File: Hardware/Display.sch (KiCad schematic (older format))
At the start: 10 parts

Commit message: [Hardware] Added buttons.
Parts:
- removed Q?: BD135, Package_TO_SOT_THT:TO-126-3_Vertical, symbol Transistor_BJT:BD135
- added Q1: DMG3414U, Package_TO_SOT_SMD:SOT-23, symbol Transistor_FET:DMG3414U
- R8: renamed from R?; value 1K -> 10K
- gave numbers to parts that had none: 7
- renumbered 10K to 10K1
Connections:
- wire segments 49 -> 53
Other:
- moved on the sheet: R8
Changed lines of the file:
@@
 $EndDescr
 $Comp
-L Transistor_BJT:BD135 Q?
-U 1 1 5E7D0088
-P 5750 5350
-F 0 "Q?" H 5941 5396 50  0000 L CNN
-F 1 "BD135" H 5941 5305 50  0000 L CNN
-F 2 "Package_TO_SOT_THT:TO-126-3_Vertical" H 5950 5275 50  0001 L CIN
-F 3 "http://www.st.com/internet/com/TECHNICAL_RESOURCES/TECHNICAL_LITERATURE/DATASHEET/CD00001225.pdf" H 5750 5350 50  0001 L CNN
-	1    5750 5350
-	-1   0    0    -1
-$EndComp
-$Comp
-L Connector:Conn_01x06_Male J?
+L Connector:Conn_01x06_Male J3
 U 1 1 5E7D0A45
 P 4500 2950
-F 0 "J?" H 4608 3331 50  0000 C CNN
+F 0 "J3" H 4608 3331 50  0000 C CNN
 F 1 "Conn_01x06_Male" H 4608 3240 50  0000 C CNN
 F 2 "" H 4500 2950 50  0001 C CNN
@@
 VDD
 $Comp
-L Connector:Conn_01x10_Male J?
+L Connector:Conn_01x10_Male J4
 U 1 1 5E7D7996
 P 4500 4050
-F 0 "J?" H 4608 4631 50  0000 C CNN
+F 0 "J4" H 4608 4631 50  0000 C CNN
 F 1 "Conn_01x10_Male" H 4608 4540 50  0000 C CNN
 F 2 "" H 4500 4050 50  0001 C CNN
@@
 LED+
 $Comp
-L power:GND #PWR?
+L power:GND #PWR0119
 U 1 1 5E7DC996
 P 5800 2400
-F 0 "#PWR?" H 5800 2150 50  0001 C CNN
+F 0 "#PWR0119" H 5800 2150 50  0001 C CNN
 F 1 "GND" H 5805 2227 50  0000 C CNN
 F 2 "" H 5800 2400 50  0001 C CNN
@@
 P 5300 2650
 AR Path="/5E7E4239" Ref="C?"  Part="1"
-AR Path="/5E7CFAFC/5E7E4239" Ref="C?"  Part="1"
-F 0 "C?" H 5415 2787 50  0000 L CNN
+AR Path="/5E7CFAFC/5E7E4239" Ref="C7"  Part="1"
+F 0 "C7" H 5415 2787 50  0000 L CNN
 F 1 "100n" H 5415 2696 50  0000 L CNN
 F 2 "Capacitor_SMD:C_1206_3216Metric_Pad1.42x1.75mm_HandSolder" H 5338 2500 50  0001 C CNN
@@
 $EndComp
 $Comp
-L Device:R_POT_TRIM 10K
+L Device:R_POT_TRIM 10K1
 U 1 1 5E7DEAB7
 P 6950 2650
-F 0 "10K" H 6880 2696 50  0000 R CNN
+F 0 "10K1" H 6880 2696 50  0000 R CNN
 F 1 "R_POT_TRIM" H 7450 2850 50  0000 R CNN
 F 2 "" H 6950 2650 50  0001 C CNN
@@
 P 5800 2650
 AR Path="/5E7EC9B4" Ref="C?"  Part="1"
-AR Path="/5E7CFAFC/5E7EC9B4" Ref="C?"  Part="1"
-F 0 "C?" H 5915 2787 50  0000 L CNN
+AR Path="/5E7CFAFC/5E7EC9B4" Ref="C8"  Part="1"
+F 0 "C8" H 5915 2787 50  0000 L CNN
 F 1 "470n" H 5915 2696 50  0000 L CNN
 F 2 "Capacitor_SMD:C_1206_3216Metric_Pad1.42x1.75mm_HandSolder" H 5838 2500 50  0001 C CNN
@@
 $EndComp
 $Comp
-L Device:CP C?
+L Device:CP C9
 U 1 1 5E7EE2A7
 P 6300 2650
-F 0 "C?" H 6182 2559 50  0000 R CNN
+F 0 "C9" H 6182 2559 50  0000 R CNN
 F 1 "220u" H 6182 2650 50  0000 R CNN
 F 2 "" H 6338 2500 50  0001 C CNN
@@
 	7100 2850 6950 2850
 $Comp
-L power:+5V #PWR?
+L power:+5V #PWR0120
 U 1 1 5E7DD692
 P 7100 2850
-F 0 "#PWR?" H 7100 2700 50  0001 C CNN
+F 0 "#PWR0120" H 7100 2700 50  0001 C CNN
 F 1 "+5V" V 7115 2978 50  0000 L CNN
 F 2 "" H 7100 2850 50  0001 C CNN
@@
 DISPLAY_DB7
 $Comp
-L power:+5V #PWR?
+L power:+5V #PWR0121
 U 1 1 5E821DC4
 P 4850 4550
-F 0 "#PWR?" H 4850 4400 50  0001 C CNN
+F 0 "#PWR0121" H 4850 4400 50  0001 C CNN
 F 1 "+5V" V 4865 4678 50  0000 L CNN
 F 2 "" H 4850 4550 50  0001 C CNN
@@
 AR Path="/5E7ACE5B/5E82967A" Ref="R?"  Part="1"
 AR Path="/5E82967A" Ref="R?"  Part="1"
-AR Path="/5E7CFAFC/5E82967A" Ref="R?"  Part="1"
-F 0 "R?" H 5430 4804 50  0000 R CNN
+AR Path="/5E7CFAFC/5E82967A" Ref="R6"  Part="1"
+F 0 "R6" H 5430 4804 50  0000 R CNN
 F 1 "12" H 5430 4895 50  0000 R CNN
 F 2 "Resistor_SMD:R_1206_3216Metric_Pad1.42x1.75mm_HandSolder" V 5430 4850 50  0001 C CNN
@@
 	-1   0    0    1
 $EndComp
-Wire Wire Line
-	5650 5050 5650 5150
-$Comp
-L power:GND #PWR?
+$Comp
+L power:GND #PWR0122
 U 1 1 5E82B8E8
-P 5650 5650
-F 0 "#PWR?" H 5650 5400 50  0001 C CNN
-F 1 "GND" H 5655 5477 50  0000 C CNN
-F 2 "" H 5650 5650 50  0001 C CNN
-F 3 "" H 5650 5650 50  0001 C CNN
-	1    5650 5650
+P 5650 5850
+F 0 "#PWR0122" H 5650 5600 50  0001 C CNN
+F 1 "GND" H 5655 5677 50  0000 C CNN
+F 2 "" H 5650 5850 50  0001 C CNN
+F 3 "" H 5650 5850 50  0001 C CNN
+	1    5650 5850
 	1    0    0    -1
 $EndComp
@@
 L Device:R R?
 U 1 1 5E82D0F5
-P 6200 5350
+P 6150 5600
 AR Path="/5E7ACE5B/5E82D0F5" Ref="R?"  Part="1"
 AR Path="/5E82D0F5" Ref="R?"  Part="1"
-AR Path="/5E7CFAFC/5E82D0F5" Ref="R?"  Part="1"
-F 0 "R?" V 6407 5350 50  0000 C CNN
-F 1 "1K" V 6316 5350 50  0000 C CNN
-F 2 "Resistor_SMD:R_1206_3216Metric_Pad1.42x1.75mm_HandSolder" V 6130 5350 50  0001 C CNN
-F 3 "~" H 6200 5350 50  0001 C CNN
-	1    6200 5350
-	0    -1   -1   0
-$EndComp
-Wire Wire Line
-	5950 5350 6050 5350
-Text HLabel 6500 5350 2    50   Input ~ 0
+AR Path="/5E7CFAFC/5E82D0F5" Ref="R8"  Part="1"
+F 0 "R8" H 6220 5646 50  0000 L CNN
+F 1 "10K" H 6220 5555 50  0000 L CNN
+F 2 "Resistor_SMD:R_1206_3216Metric_Pad1.42x1.75mm_HandSolder" V 6080 5600 50  0001 C CNN
+F 3 "~" H 6150 5600 50  0001 C CNN
+	1    6150 5600
+	1    0    0    -1
+$EndComp
+Text HLabel 6500 5400 2    50   Input ~ 0
 DISPLAY_BACKLIGHT
 Wire Wire Line
-	6350 5350 6500 5350
-Wire Wire Line
-	5650 5550 5650 5650
+	5650 5600 5650 5800
 $Comp
 L Device:R R?
@@
 AR Path="/5E7ACE5B/5E836C01" Ref="R?"  Part="1"
 AR Path="/5E836C01" Ref="R?"  Part="1"
-AR Path="/5E7CFAFC/5E836C01" Ref="R?"  Part="1"
-F 0 "R?" H 5730 4804 50  0000 R CNN
+AR Path="/5E7CFAFC/5E836C01" Ref="R7"  Part="1"
+F 0 "R7" H 5730 4804 50  0000 R CNN
 F 1 "12" H 5730 4895 50  0000 R CNN
 F 2 "Resistor_SMD:R_1206_3216Metric_Pad1.42x1.75mm_HandSolder" V 5730 4850 50  0001 C CNN
@@
 Text Notes 6400 4950 0    50   ~ 0
 Backlight leds forward voltage is about 4 to 4.5V.\nBacklight leds maximum current is 200mA.\nWith 6 ohm resistor, maximum current will be\nbetween (5-4)/6 = 166mA and (5-4.5)/6 = 83mA.\nResistors dissipated power is between\n(5-4)²/6 = 166mW and (5-4.5)²/6 = 42mW,\nso allow up to 500mW to be dissipated to be sure.
+$Comp
+L Transistor_FET:DMG3414U Q1
+U 1 1 5E7C7532
+P 5750 5400
+F 0 "Q1" H 5956 5446 50  0000 L CNN
+F 1 "DMG3414U" H 5956 5355 50  0000 L CNN
+F 2 "Package_TO_SOT_SMD:SOT-23" H 5950 5325 50  0001 L CIN
+F 3 "http://www.diodes.com/assets/Datasheets/ds31739.pdf" H 5750 5400 50  0001 L CNN
+	1    5750 5400
+	-1   0    0    -1
+$EndComp
+Wire Wire Line
+	5650 5800 6150 5800
+Wire Wire Line
+	6150 5800 6150 5750
+Connection ~ 5650 5800
+Wire Wire Line
+	5650 5800 5650 5850
+Wire Wire Line
+	5950 5400 6150 5400
+Wire Wire Line
+	6150 5400 6150 5450
+Wire Wire Line
+	6150 5400 6500 5400
+Connection ~ 6150 5400
+Wire Wire Line
+	5650 5050 5650 5200
 $EndSCHEMATC

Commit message: [Hardware] Added all schematic parts (but not all external parts, like display or female connectors).
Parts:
- C8: value 470n -> 4.7u
- C9: footprint (none) -> Capacitor_SMD:CP_Elec_8x10.5
- J3: footprint (none) -> Connector_PinHeader_2.54mm:PinHeader_1x06_P2.54mm_Vertical
- J4: footprint (none) -> Connector_PinHeader_2.54mm:PinHeader_1x10_P2.54mm_Vertical
- RV1: renamed from 10K1; value R_POT_TRIM -> 10K; footprint (none) -> Potentiometer_SMD:Potentiometer_Bourns_3314J_Vertical; Champ4 (none) -> Bourns 3314J-1-103E
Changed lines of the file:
@@
 $Descr A4 11693 8268
 encoding utf-8
-Sheet 4 3
+Sheet 3 3
 Title "4 lines x 20 characters LCD display"
 Date ""
@@
 F 0 "J3" H 4608 3331 50  0000 C CNN
 F 1 "Conn_01x06_Male" H 4608 3240 50  0000 C CNN
-F 2 "" H 4500 2950 50  0001 C CNN
+F 2 "Connector_PinHeader_2.54mm:PinHeader_1x06_P2.54mm_Vertical" H 4500 2950 50  0001 C CNN
 F 3 "~" H 4500 2950 50  0001 C CNN
 	1    4500 2950
@@
 F 0 "J4" H 4608 4631 50  0000 C CNN
 F 1 "Conn_01x10_Male" H 4608 4540 50  0000 C CNN
-F 2 "" H 4500 4050 50  0001 C CNN
+F 2 "Connector_PinHeader_2.54mm:PinHeader_1x10_P2.54mm_Vertical" H 4500 4050 50  0001 C CNN
 F 3 "~" H 4500 4050 50  0001 C CNN
 	1    4500 4050
@@
 $EndComp
 $Comp
-L Device:R_POT_TRIM 10K1
+L Device:R_POT_TRIM RV1
 U 1 1 5E7DEAB7
 P 6950 2650
-F 0 "10K1" H 6880 2696 50  0000 R CNN
-F 1 "R_POT_TRIM" H 7450 2850 50  0000 R CNN
-F 2 "" H 6950 2650 50  0001 C CNN
+F 0 "RV1" H 6881 2741 50  0000 R CNN
+F 1 "10K" H 6881 2650 50  0000 R CNN
+F 2 "Potentiometer_SMD:Potentiometer_Bourns_3314J_Vertical" H 6950 2650 50  0001 C CNN
 F 3 "~" H 6950 2650 50  0001 C CNN
+F 4 "Bourns 3314J-1-103E" H 7900 2800 50  0000 R CNN "Champ4"
 	1    6950 2650
 	1    0    0    -1
@@
 AR Path="/5E7CFAFC/5E7EC9B4" Ref="C8"  Part="1"
 F 0 "C8" H 5915 2787 50  0000 L CNN
-F 1 "470n" H 5915 2696 50  0000 L CNN
+F 1 "4.7u" H 5915 2696 50  0000 L CNN
 F 2 "Capacitor_SMD:C_1206_3216Metric_Pad1.42x1.75mm_HandSolder" H 5838 2500 50  0001 C CNN
 F 3 "~" H 5800 2650 50  0001 C CNN
@@
 F 0 "C9" H 6182 2559 50  0000 R CNN
 F 1 "220u" H 6182 2650 50  0000 R CNN
-F 2 "" H 6338 2500 50  0001 C CNN
+F 2 "Capacitor_SMD:CP_Elec_8x10.5" H 6338 2500 50  0001 C CNN
 F 3 "~" H 6300 2650 50  0001 C CNN
 F 4 "25V" H 6182 2741 50  0000 R CNN "Champ4"

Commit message: [Hardware] Started PCB routing. Components are placed, BME680 board mounting holes are in position, some nets are connected.
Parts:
- J3: value Conn_01x06_Male -> Display_1
- J4: value Conn_01x10_Male -> Display_2
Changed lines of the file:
@@
 P 4500 2950
 F 0 "J3" H 4608 3331 50  0000 C CNN
-F 1 "Conn_01x06_Male" H 4608 3240 50  0000 C CNN
+F 1 "Display_1" H 4608 3240 50  0000 C CNN
 F 2 "Connector_PinHeader_2.54mm:PinHeader_1x06_P2.54mm_Vertical" H 4500 2950 50  0001 C CNN
 F 3 "~" H 4500 2950 50  0001 C CNN
@@
 P 4500 4050
 F 0 "J4" H 4608 4631 50  0000 C CNN
-F 1 "Conn_01x10_Male" H 4608 4540 50  0000 C CNN
+F 1 "Display_2" H 4608 4540 50  0000 C CNN
 F 2 "Connector_PinHeader_2.54mm:PinHeader_1x10_P2.54mm_Vertical" H 4500 4050 50  0001 C CNN
 F 3 "~" H 4500 4050 50  0001 C CNN

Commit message: [Hardware] Moved buttons to another schematic sheet and fully routed PCB.
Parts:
- C9: Champ6 (none) -> Panasonic EEEFK1E221P
- RV1: Champ4 Bourns 3314J-1-103E -> (none); Champ6 (none) -> Bourns 3314J-1-103E
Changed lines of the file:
@@
 $Descr A4 11693 8268
 encoding utf-8
-Sheet 3 3
+Sheet 3 4
 Title "4 lines x 20 characters LCD display"
 Date ""
@@
 F 2 "Potentiometer_SMD:Potentiometer_Bourns_3314J_Vertical" H 6950 2650 50  0001 C CNN
 F 3 "~" H 6950 2650 50  0001 C CNN
-F 4 "Bourns 3314J-1-103E" H 7900 2800 50  0000 R CNN "Champ4"
+F 4 "Bourns 3314J-1-103E" H 7900 2800 50  0000 R CNN "Champ6"
 	1    6950 2650
 	1    0    0    -1
@@
 F 3 "~" H 6300 2650 50  0001 C CNN
 F 4 "25V" H 6182 2741 50  0000 R CNN "Champ4"
+F 5 "Panasonic EEEFK1E221P" H 6300 2650 50  0001 C CNN "Champ6"
 	1    6300 2650
 	-1   0    0    1

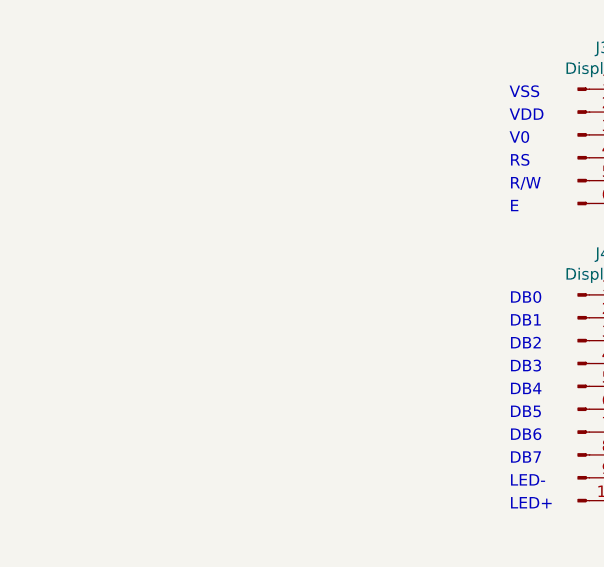
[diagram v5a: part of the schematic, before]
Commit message: [Hardware] Added display part in both schematic and PCB.
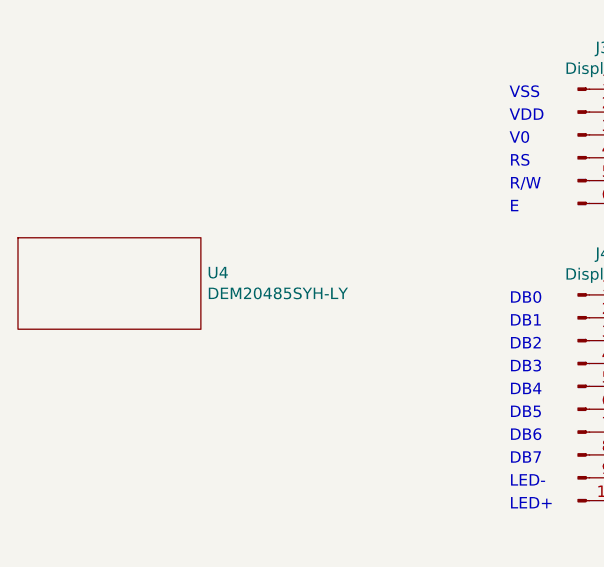
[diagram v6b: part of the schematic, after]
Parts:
- added U4: DEM20485SYH-LY, Empty_Footprint:Empty_Footprint, symbol LCD_Display:DEM20485SYH-LY
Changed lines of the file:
@@
 Wire Wire Line
 	5650 5050 5650 5200
+$Comp
+L LCD_Display:DEM20485SYH-LY U4
+U 1 1 5E7D0A49
+P 2450 3600
+F 0 "U4" H 2878 3646 50  0000 L CNN
+F 1 "DEM20485SYH-LY" H 2878 3555 50  0000 L CNN
+F 2 "Empty_Footprint:Empty_Footprint" H 2450 3600 50  0001 C CNN
+F 3 "" H 2450 3600 50  0001 C CNN
+	1    2450 3600
+	1    0    0    -1
+$EndComp
 $EndSCHEMATC

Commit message: [Hardware] Renamed LCD display symbol for more coherency.
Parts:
- U4: value DEM20485SYH-LY -> DEM20485SYH-LY_Supply; symbol LCD_Display:DEM20485SYH-LY -> LCD_Display:DEM20485SYH-LY_Supply
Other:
- moved on the sheet: U4
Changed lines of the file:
@@
 	5650 5050 5650 5200
 $Comp
-L LCD_Display:DEM20485SYH-LY U4
+L LCD_Display:DEM20485SYH-LY_Supply U4
 U 1 1 5E7D0A49
-P 2450 3600
-F 0 "U4" H 2878 3646 50  0000 L CNN
-F 1 "DEM20485SYH-LY" H 2878 3555 50  0000 L CNN
-F 2 "Empty_Footprint:Empty_Footprint" H 2450 3600 50  0001 C CNN
-F 3 "" H 2450 3600 50  0001 C CNN
-	1    2450 3600
+P 1850 3550
+F 0 "U4" H 2278 3596 50  0000 L CNN
+F 1 "DEM20485SYH-LY_Supply" H 2278 3505 50  0000 L CNN
+F 2 "Empty_Footprint:Empty_Footprint" H 1850 3550 50  0001 C CNN
+F 3 "" H 1850 3550 50  0001 C CNN
+	1    1850 3550
 	1    0    0    -1
 $EndComp

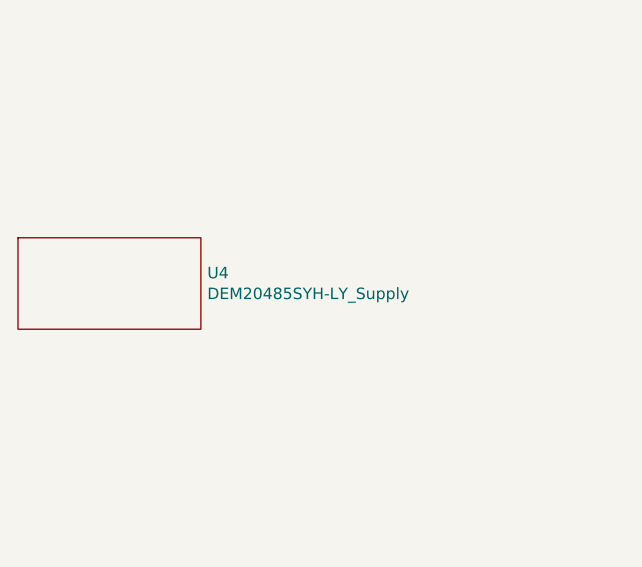
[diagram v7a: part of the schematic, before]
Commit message: [Hardware] Replaced each supply part by a generic one to avoid creating a new symbol for every supply part.
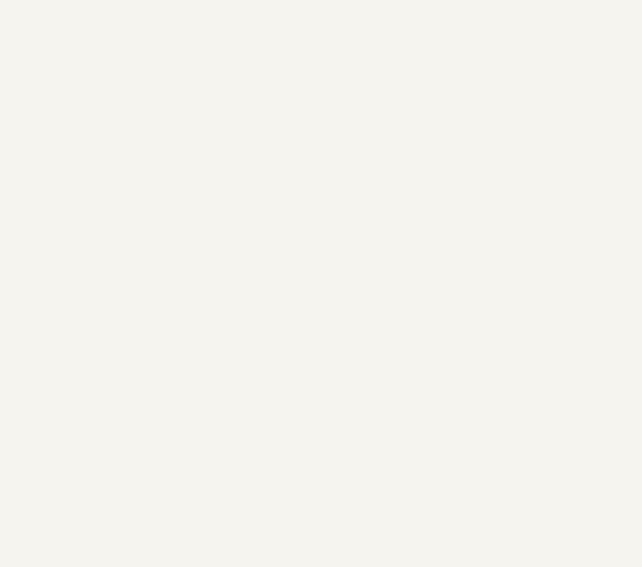
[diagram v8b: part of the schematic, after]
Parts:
- removed U4: DEM20485SYH-LY_Supply, Empty_Footprint:Empty_Footprint, symbol LCD_Display:DEM20485SYH-LY_Supply
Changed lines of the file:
@@
 $Descr A4 11693 8268
 encoding utf-8
-Sheet 3 4
+Sheet 3 5
 Title "4 lines x 20 characters LCD display"
 Date ""
@@
 Wire Wire Line
 	5650 5050 5650 5200
-$Comp
-L LCD_Display:DEM20485SYH-LY_Supply U4
-U 1 1 5E7D0A49
-P 1850 3550
-F 0 "U4" H 2278 3596 50  0000 L CNN
-F 1 "DEM20485SYH-LY_Supply" H 2278 3505 50  0000 L CNN
-F 2 "Empty_Footprint:Empty_Footprint" H 1850 3550 50  0001 C CNN
-F 3 "" H 1850 3550 50  0001 C CNN
-	1    1850 3550
-	1    0    0    -1
-$EndComp
 $EndSCHEMATC
